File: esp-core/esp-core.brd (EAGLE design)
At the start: 35.6 x 35.6 mm, 6 parts

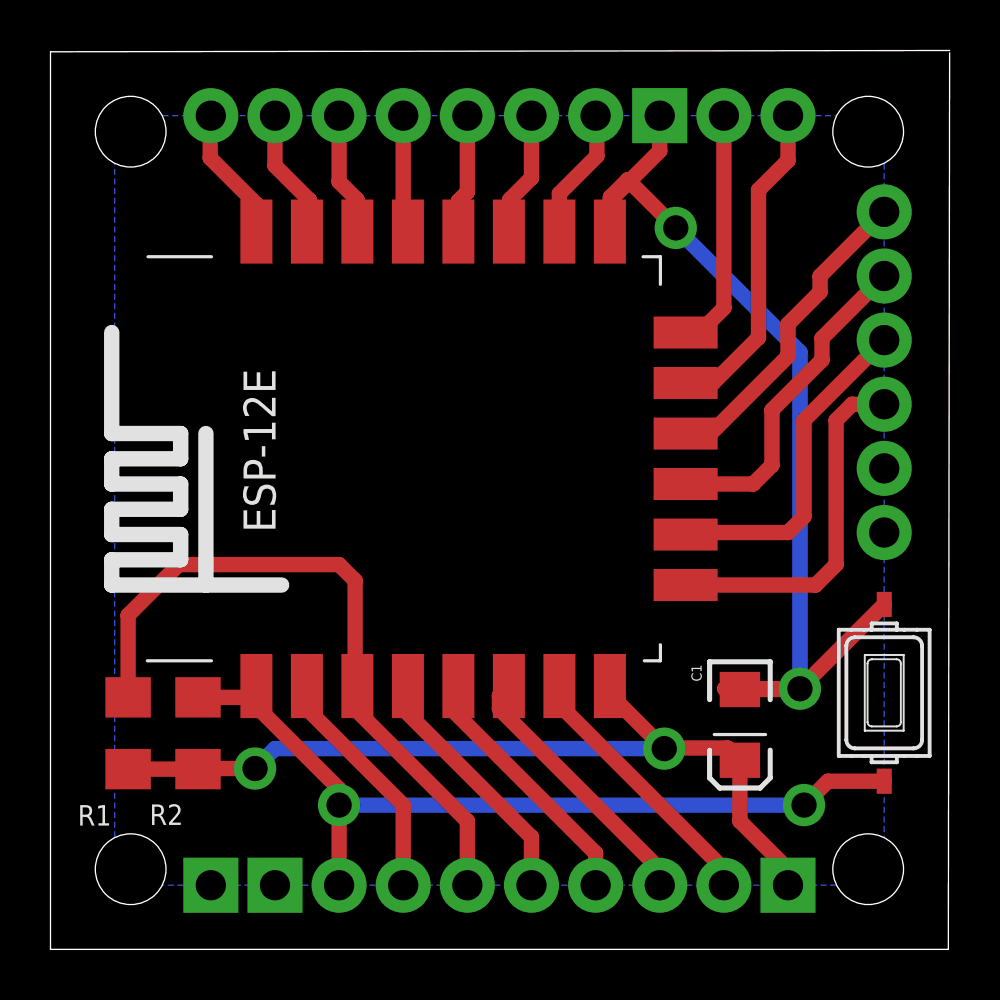
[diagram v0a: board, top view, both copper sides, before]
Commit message: Add pull-up and down resistors to 'special' pins - GPIO0 and GPIO15
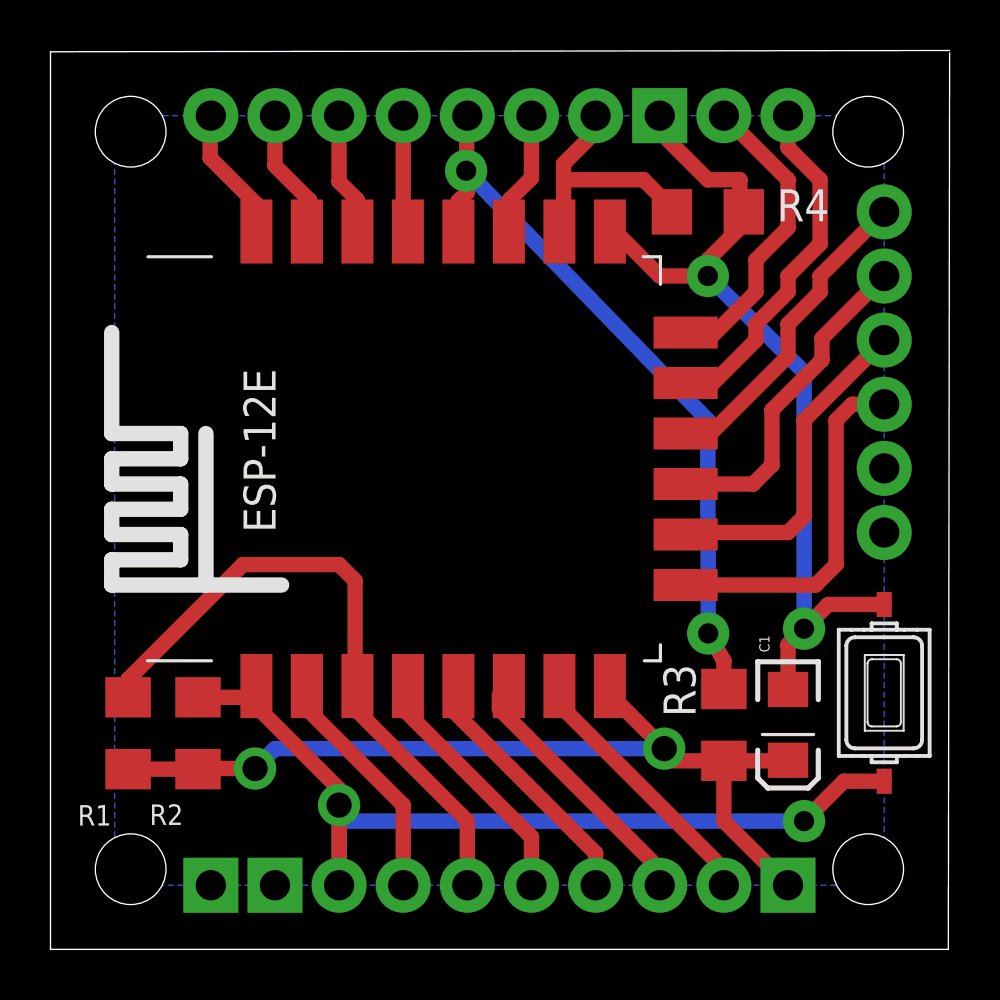
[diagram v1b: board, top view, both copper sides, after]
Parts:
- added R3, R4: 10k, dp_devices:R1206
- moved C1 1.91 mm to (29.2, 8.89)
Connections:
- net +3V3: now also R3.2
- net GND: now also R4.1
- net GPIO0: now also R3.1
- net GPIO15: now also R4.2
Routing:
- net GPIO0: track 4.74 -> 29.3 mm, vias 0 -> 2
- net GPIO15: track 5.23 -> 10.1 mm
- net GND: track 40.2 -> 36.1 mm
- net RESET: track 33.7 -> 36.5 mm
- net SCLK: track 9.54 -> 12.3 mm
- net +3V3: track 34.7 -> 37.1 mm
- net EN: track 27.3 -> 25.8 mm
- net MOSI: track 12.9 -> 14.1 mm

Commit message: Fix small DRC issues with esp-core board
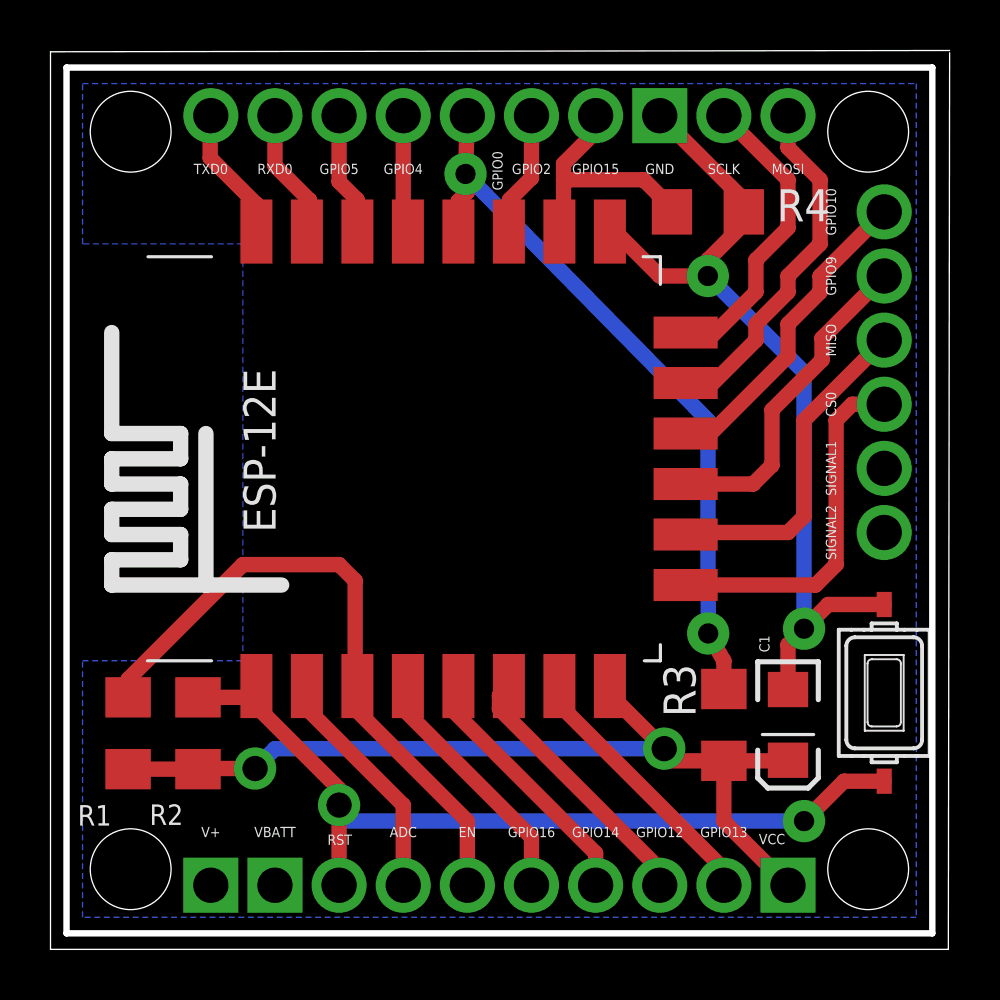
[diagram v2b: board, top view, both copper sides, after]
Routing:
- net RESET: track 36.5 -> 34.0 mm
- net GND: track 36.1 -> 35.4 mm
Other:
- outline, holes or cut-outs redrawn
- board text added: "ADC"
- board text added: "CS0"
- board text added: "EN"
- board text added: "GND"
- board text added: "GPIO0"
- board text added: "GPIO10"
- board text added: "GPIO12"
- board text added: "GPIO13"
- board text added: "GPIO14"
- board text added: "GPIO15"
- board text added: "GPIO16"
- board text added: "GPIO2"
- board text added: "GPIO4"
- board text added: "GPIO5"
- board text added: "GPIO9"
- board text added: "MISO"
- board text added: "MOSI"
- board text added: "RST"
- board text added: "RXD0"
- board text added: "SCLK"
- board text added: "SIGNAL1"
- board text added: "SIGNAL2"
- board text added: "TXD0"
- board text added: "V+"
- board text added: "VBATT"
- board text added: "VCC"

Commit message: Fix button on board
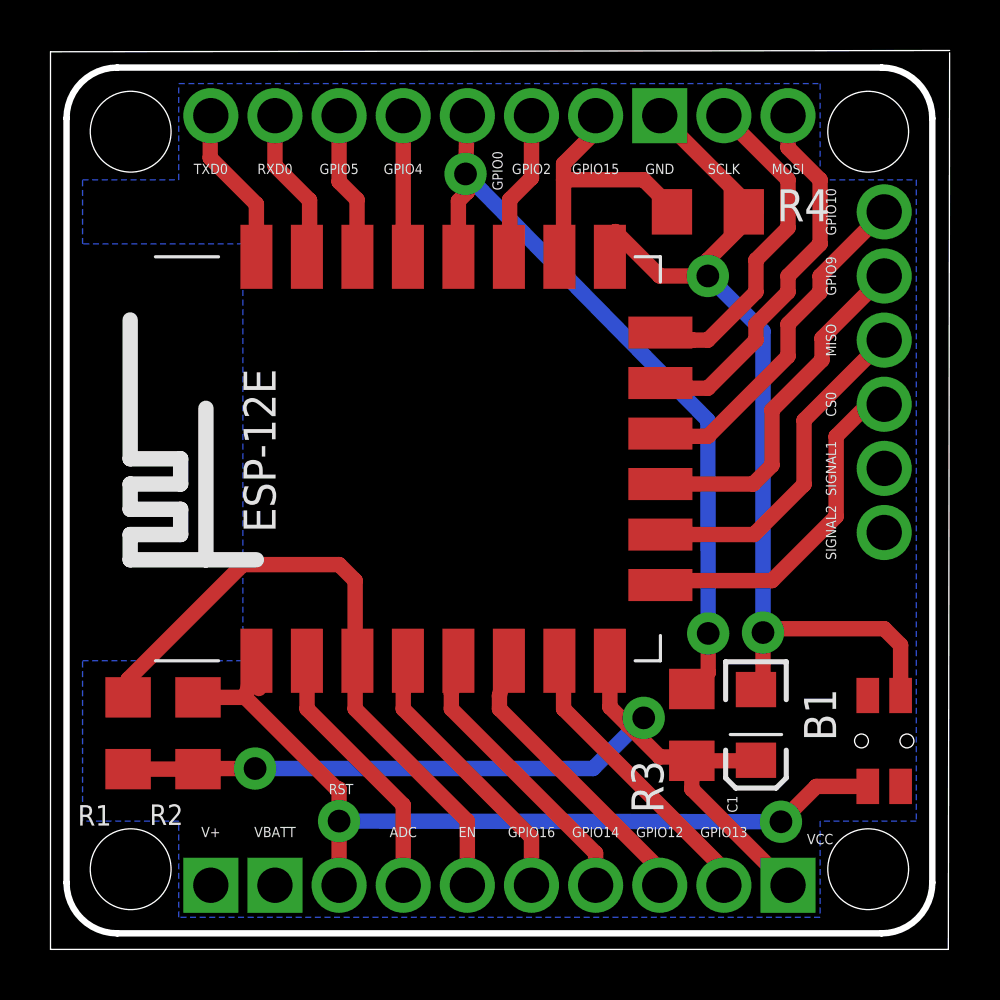
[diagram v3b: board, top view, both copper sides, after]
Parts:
- removed RESET: SW_TACT_2P-3X6, dp_devices:SW_TACT_3X6
- added B1: (no value), ESPstack:SKSCLDE010
- moved R3 1.27 mm to (25.4, 8.89)
- moved C1 1.27 mm to (27.9, 8.89)
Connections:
- net CS0: now also ESP-12E.CS0; no longer ESP-12E.CSO
- net GND: now also B1.1, B1.2; no longer RESET.1
- net RESET: now also B1.3, B1.4; no longer RESET.2
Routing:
- net GND: track 35.4 -> 39.6 mm
- net EN: track 25.8 -> 27.6 mm
- net GPIO0: track 29.2 -> 30.3 mm
- net RESET: track 34.0 -> 35.0 mm
- net TXD0: track 5.36 -> 6.36 mm
- net GPIO9: track 13.1 -> 14.1 mm
- net ADC: track 9.47 -> 10.5 mm
- net GPIO5: track 4.89 -> 5.88 mm
- net GPIO2: track 4.96 -> 5.95 mm
- net RXD0: track 5.20 -> 6.16 mm
- net GPIO10: track 12.7 -> 13.7 mm
- net GPIO15: track 10.1 -> 11.0 mm
- net GPIO13: track 10.6 -> 11.5 mm
- net GPIO4: track 4.67 -> 5.60 mm
- net GPIO16: track 10.1 -> 11.0 mm
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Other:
- outline, holes or cut-outs redrawn

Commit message: Add openhardware icon to library and to core board
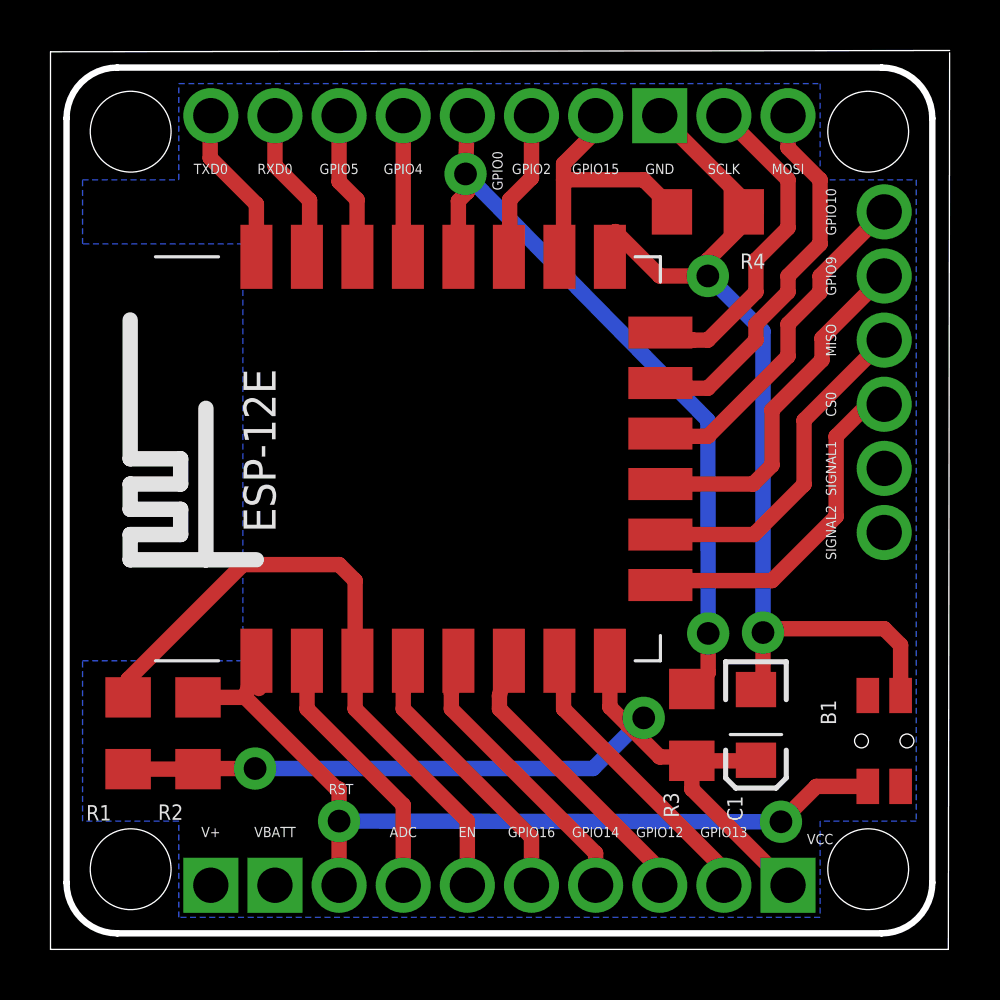
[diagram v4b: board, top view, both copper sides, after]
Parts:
- added U$1: (no value), ESPstack:OSHW2
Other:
- board text added: "prototype rev. 0.1"
